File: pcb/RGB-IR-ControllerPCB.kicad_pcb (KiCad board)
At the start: 2 copper layers, 52.5 x 64.5 mm, 14 parts, among them J1 Screw_Terminal_01x02, J2 Screw_Terminal_01x04, Q1 IRF540N, Q2 IRF540N, Q3 IRF540N, U1 TSOP17xx, U2 L7805

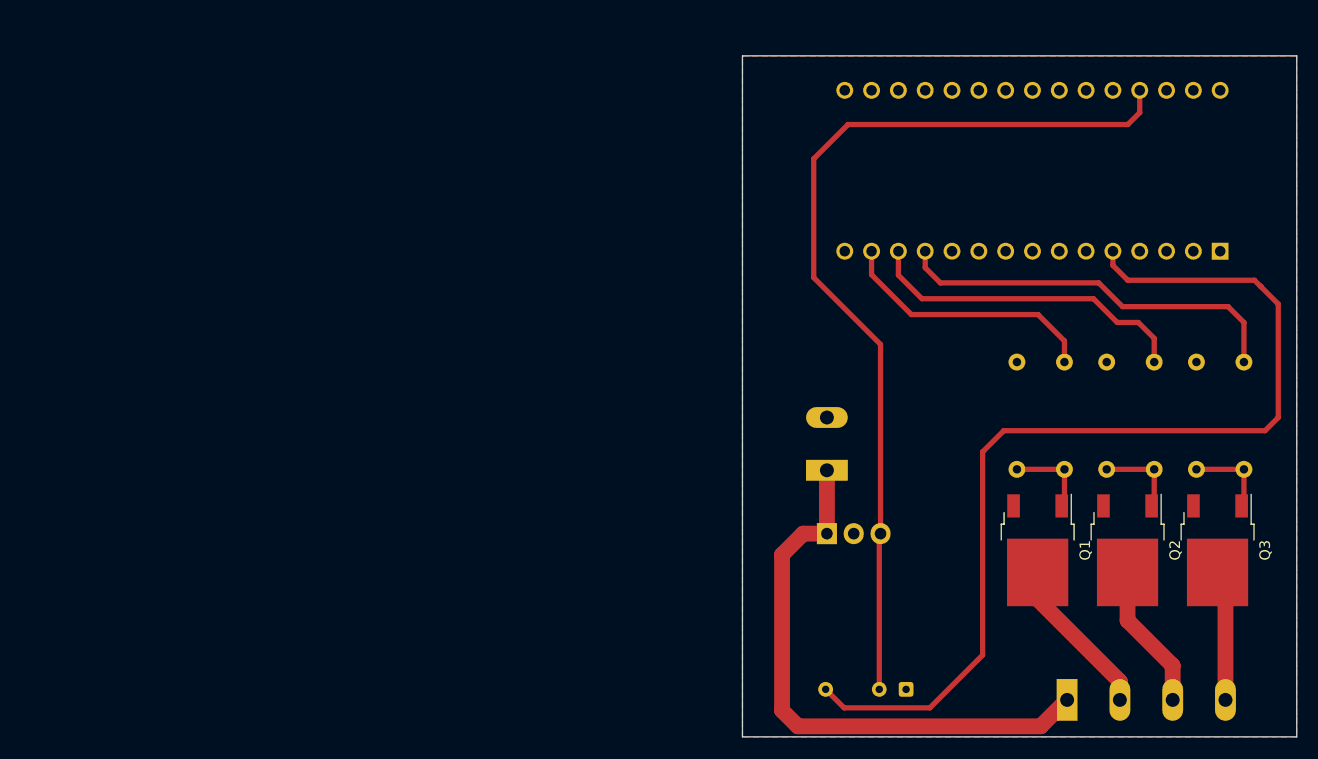
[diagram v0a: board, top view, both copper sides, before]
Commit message: PCB prototype without GND connection
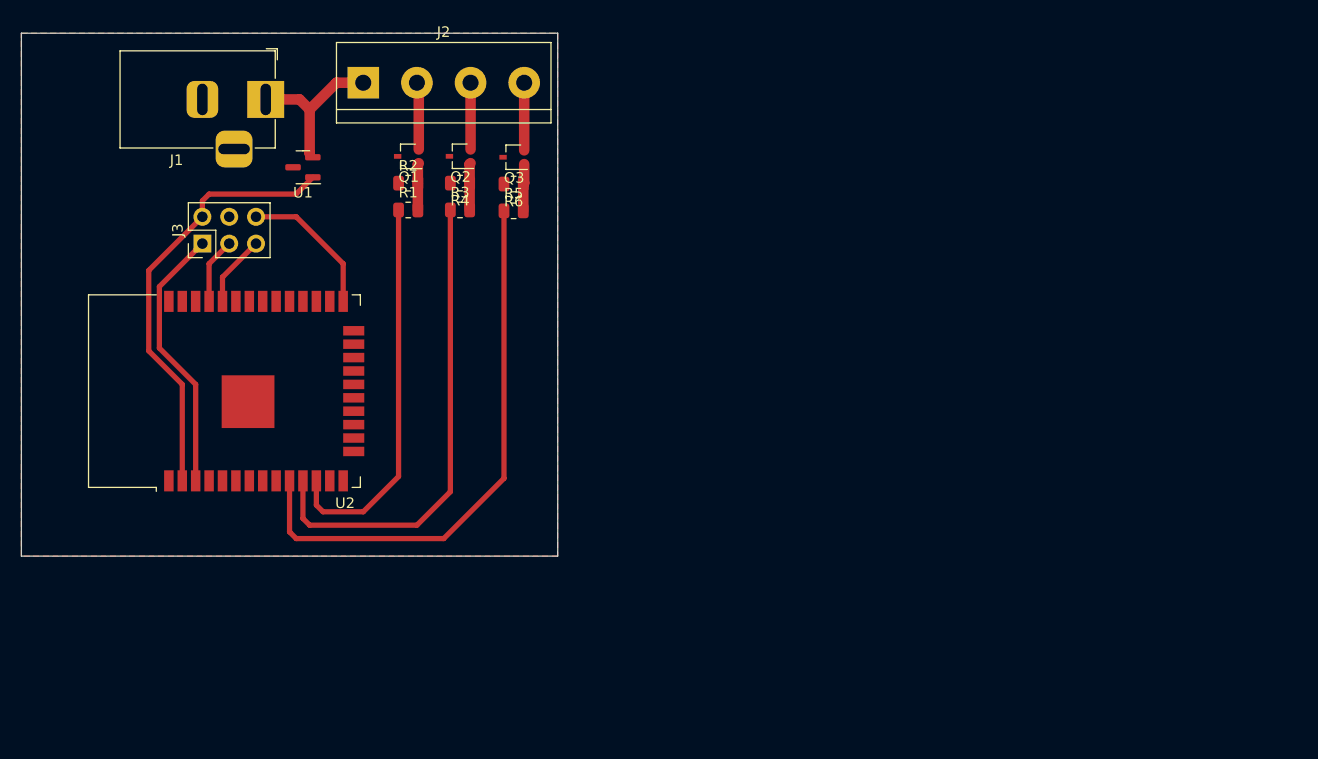
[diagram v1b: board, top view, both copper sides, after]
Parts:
- removed A1: Arduino_Nano_v3.x, Module:Arduino_Nano
- added J3: UART, Connector_PinHeader_2.54mm:PinHeader_2x03_P2.54mm_Vertical, F.Cu at (39.8, 36.3)
- J1: value Screw_Terminal_01x02 -> Barrel_Jack; footprint TerminalBlock:TerminalBlock_Altech_AK300-2_P5.00mm -> Connector_BarrelJack:BarrelJack_Horizontal; moved to F.Cu
- J2: value Screw_Terminal_01x04 -> RGB_WIRES; footprint TerminalBlock:TerminalBlock_Altech_AK300-4_P5.00mm -> TerminalBlock:TerminalBlock_bornier-4_P5.08mm; moved to F.Cu
- Q1, Q2, Q3: footprint Package_TO_SOT_SMD:TO-252-2 -> Package_TO_SOT_SMD:SOT-323_SC-70
- R1, R2, R3, R4, R5, R6: footprint Resistor_THT:R_Axial_DIN0207_L6.3mm_D2.5mm_P10.16mm_Horizontal -> Resistor_SMD:R_0805_2012Metric; moved to F.Cu
- U1: value TSOP17xx -> LM3480-3.3; footprint OptoDevice:Vishay_CAST-3Pin -> Package_TO_SOT_SMD:SOT-23; moved to F.Cu
- U2: value L7805 -> ESP32-WROOM-32D; footprint Package_TO_SOT_THT:TO-220-3_Vertical -> RF_Module:ESP32-WROOM-32; moved to F.Cu
- moved J2 88.7 mm to (55.1, 21.0)
- moved Q3 76.4 mm to (69.3, 28.1), turned to 180 degrees
- moved U1 75.6 mm to (49.4, 29.1)
- moved Q2 73.4 mm to (64.2, 28.0), turned to 180 degrees
- moved R5 70.6 mm to (69.3, 33.2), turned to 0 degrees
- moved Q1 70.3 mm to (59.3, 28.0), turned to 180 degrees
- moved R3 67.3 mm to (64.2, 33.1), turned to 0 degrees
- moved R6 66.8 mm to (69.3, 30.6), turned to 180 degrees
- moved R1 63.8 mm to (59.3, 33.1), turned to 0 degrees
- moved J1 63.7 mm to (45.8, 22.6), turned to 0 degrees
- moved R4 63.6 mm to (64.2, 30.6), turned to 180 degrees
- moved R2 60.1 mm to (59.3, 30.6), turned to 0 degrees
- moved U2 55.7 mm to (44.9, 50.2), turned to 90 degrees
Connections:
- net Net-(J2-Pad2) renamed GREEN_WIRE
- net Net-(J2-Pad3) renamed RED_WIRE
- net Net-(J2-Pad4) renamed BLUE_WIRE
- Q3 pad 1: Net-(Q3-Pad1) -> Net-(R6-Pad1)
- R4 pad 1: GND -> Net-(Q2-Pad1)
- R4 pad 2: Net-(Q2-Pad1) -> GND
- R5 pad 2: Net-(Q3-Pad1) -> Net-(R6-Pad1)
- R6 pad 1: GND -> Net-(R6-Pad1)
- R6 pad 2: Net-(Q3-Pad1) -> GND
- U1 pad 1: GND -> +3.3V
- U1 pad 2: +5V -> +12V
- U1 pad 3: IR_DATA_OUT -> GND
- U2 pad 1: +12V -> GND
- U2 pad 2: GND -> +3.3V
- U2 pad 3: +5V -> ESP_EN
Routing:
- net IR_DATA_OUT: track 95.7 -> 0.00 mm
- net +5V: track 87.7 -> 0.00 mm
- net +3.3V: track 0.00 -> 41.3 mm
- net +12V: track 54.5 -> 14.8 mm
- net ESP_EN: track 0.00 -> 25.6 mm
- net BLUE_PIN: track 37.6 -> 53.1 mm
- net RED_PIN: track 31.2 -> 45.8 mm
- net ESP_BOOT: track 0.00 -> 13.7 mm
- net GREEN_WIRE: track 18.5 -> 6.40 mm
- net GREEN_PIN: track 25.1 -> 37.0 mm
- net Net-(Q3-Pad1): track 8.06 -> 0.00 mm
- net RED_WIRE: track 13.8 -> 6.32 mm
- net ESP_RXD: track 0.00 -> 6.79 mm
- net ESP_TXD: track 0.00 -> 6.26 mm
- net BLUE_WIRE: track 12.4 -> 6.41 mm
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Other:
- board size 52.5 x 64.5 mm -> 50.8 x 49.5 mm
- net class Default removed
